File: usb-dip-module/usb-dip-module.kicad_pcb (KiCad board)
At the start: 2 copper layers, 10.2 x 17.8 mm, 9 parts, among them CON1 USB-MINI-B, P1 CONN_4, P2 CONN_4, U1 TPD2E001IDRLRQ1, U2 AAT3220

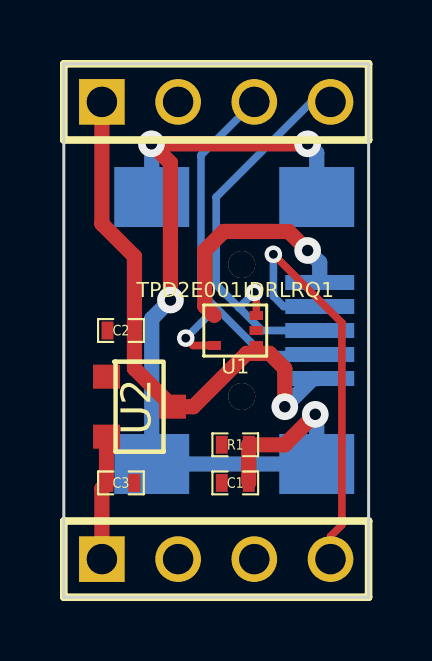
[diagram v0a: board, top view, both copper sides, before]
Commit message: squeezed USB DIP module 100 mils narrower
SMT stencils from previous version should still work, though the
USB connector shield is very slightly narrower to clear the header
through-holes (IIRC, i only had to trim about 1 mil off so it
should be fine)
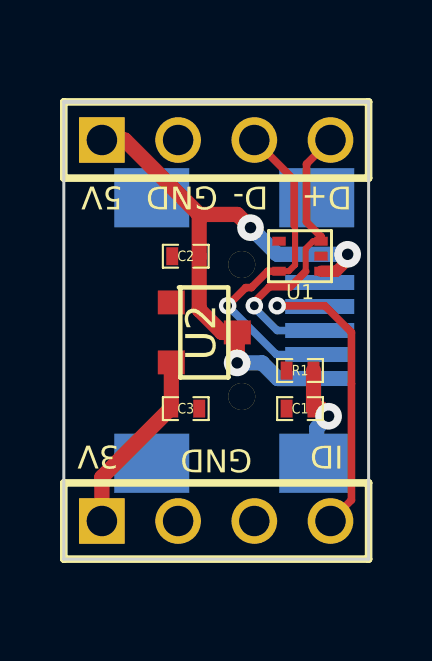
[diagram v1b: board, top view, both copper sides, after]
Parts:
- moved C1 3.29 mm to (190.8, 139.8)
- moved C3 3.29 mm to (186.9, 139.8)
- moved C2 3.29 mm to (186.9, 134.7)
- moved R1 3.29 mm to (190.8, 138.5)
- moved U1 3.29 mm to (190.8, 134.7)
- moved U2 3.29 mm to (188.2, 137.2)
- moved P1 1.27 mm to (188.0, 143.5)
- moved P2 1.27 mm to (188.0, 130.8)
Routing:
- net N-000003: track 31.2 -> 3.61 mm, vias 4 -> 1
- net GND: track 7.49 -> 0.00 mm, vias 1 -> 0
- net D+: track 13.6 -> 10.1 mm
- net ID: track 14.3 -> 10.8 mm
- net D-: track 14.4 -> 11.3 mm
- net VREG: track 4.14 -> 6.24 mm
- net VBUS: track 18.6 -> 19.7 mm, vias 1 -> 3
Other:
- board size 10.2 x 17.8 mm -> 10.2 x 15.2 mm
- rule trace_min: 0.254 -> 0.1524
- board text added: "3V"
- board text added: "5V"
- board text removed: "+3.3V"
- board text removed: "+5V"

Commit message: changed usb DIP module to use what should be OSH Park-friendly NPTH's
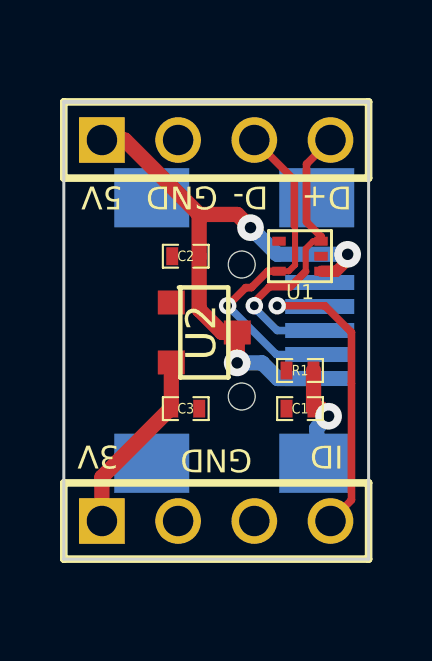
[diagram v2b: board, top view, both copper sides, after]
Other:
- rule trace_min: 0.1524 -> 0.006
- rule via_min_size: 0.508 -> 0.02
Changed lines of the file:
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@@
   (page A3)
   (layers
-    (15 F.Cu signal)
+    (15 F.Cu signal hide)
     (0 B.Cu signal)
-    (16 B.Adhes user)
-    (17 F.Adhes user)
-    (18 B.Paste user)
-    (19 F.Paste user)
-    (20 B.SilkS user)
-    (21 F.SilkS user)
+    (16 B.Adhes user hide)
+    (17 F.Adhes user hide)
+    (18 B.Paste user hide)
+    (19 F.Paste user hide)
+    (20 B.SilkS user hide)
+    (21 F.SilkS user hide)
     (22 B.Mask user)
     (23 F.Mask user)
@@
     (zone_clearance 0.1524)
     (zone_45_only no)
-    (trace_min 0.1524)
+    (trace_min 0.006)
     (segment_width 0.2)
     (edge_width 0.1)
     (via_size 0.5842)
     (via_drill 0.381)
-    (via_min_size 0.508)
+    (via_min_size 0.02)
     (via_min_drill 0.3302)
     (uvia_size 0.508)
     (uvia_drill 0.127)
     (uvias_allowed no)
-    (uvia_min_size 0.508)
+    (uvia_min_size 0.02)
     (uvia_min_drill 0.127)
     (pcb_text_width 0.3)
@@
     (mod_text_size 1 1)
     (mod_text_width 0.15)
-    (pad_size 2.49936 1.97358)
-    (pad_drill 0)
+    (pad_size 0.89916 0.89916)
+    (pad_drill 0.89916)
     (pad_to_mask_clearance 0)
     (aux_axis_origin 0 0)
@@
       (layers B.Cu B.Paste B.Mask)
     )
-    (pad "" thru_hole circle (at 0.8509 2.19964) (size 0.89916 0.89916) (drill 0.89916)
+    (pad "" np_thru_hole circle (at 0.8509 2.19964) (size 0.89916 0.89916) (drill 0.89916)
       (layers *.Cu *.Mask B.SilkS)
     )
-    (pad "" thru_hole circle (at 0.8509 -2.19964) (size 0.89916 0.89916) (drill 0.89916)
+    (pad "" np_thru_hole circle (at 0.8509 -2.19964) (size 0.89916 0.89916) (drill 0.89916)
       (layers *.Cu *.Mask B.SilkS)
     )

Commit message: sigh... another borked order.  removed planes, rerouted, let's try this again.
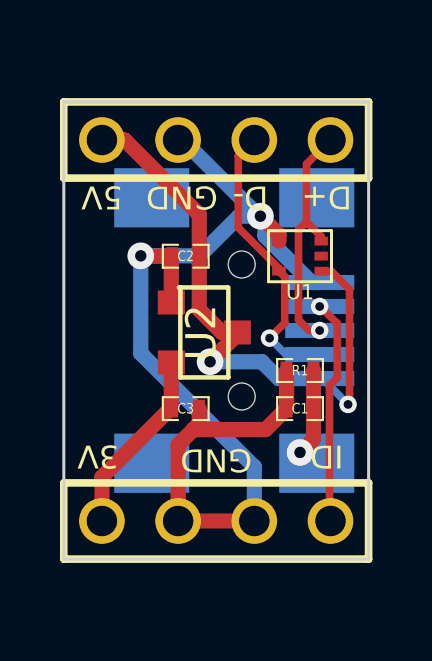
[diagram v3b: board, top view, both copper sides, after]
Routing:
- net GND: track 0.00 -> 36.9 mm, vias 0 -> 2
- net ID: track 10.8 -> 7.54 mm
- net D+: track 10.1 -> 8.13 mm
- net D-: track 11.3 -> 9.57 mm
- net VBUS: track 19.7 -> 20.6 mm, vias 3 -> 2
- removed copper zone on B.Cu, net GND
- removed copper zone on F.Cu, net GND
